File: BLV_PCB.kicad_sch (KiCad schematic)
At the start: 10 parts, among them J1 Cube0_UART_JST-PH, J2 Cube0_UART_JST-PH, J3 Cube0_UART_JST-PH, J4 Cube0_UART_Debug, J5 Cube0_UART_Debug, J6 Cube0_UART_Debug

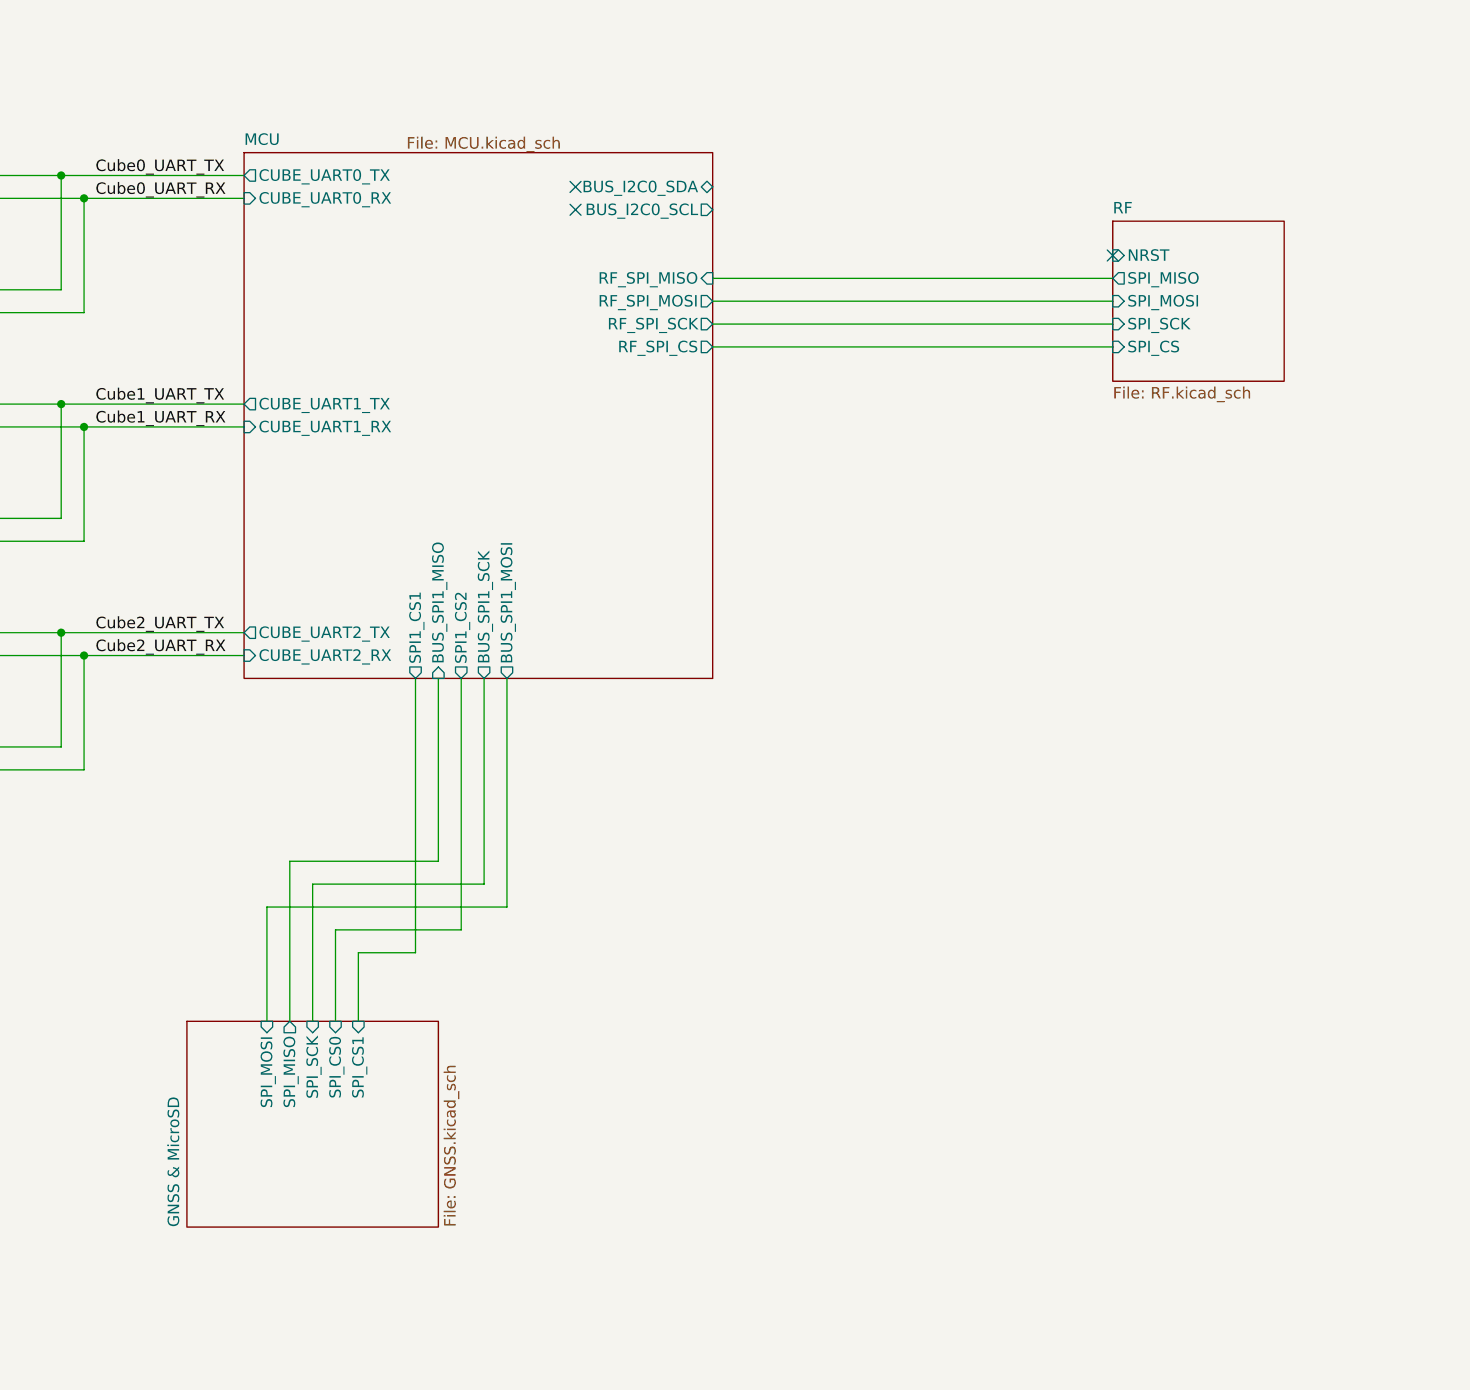
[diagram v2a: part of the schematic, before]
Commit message: Updated EBYTE placement
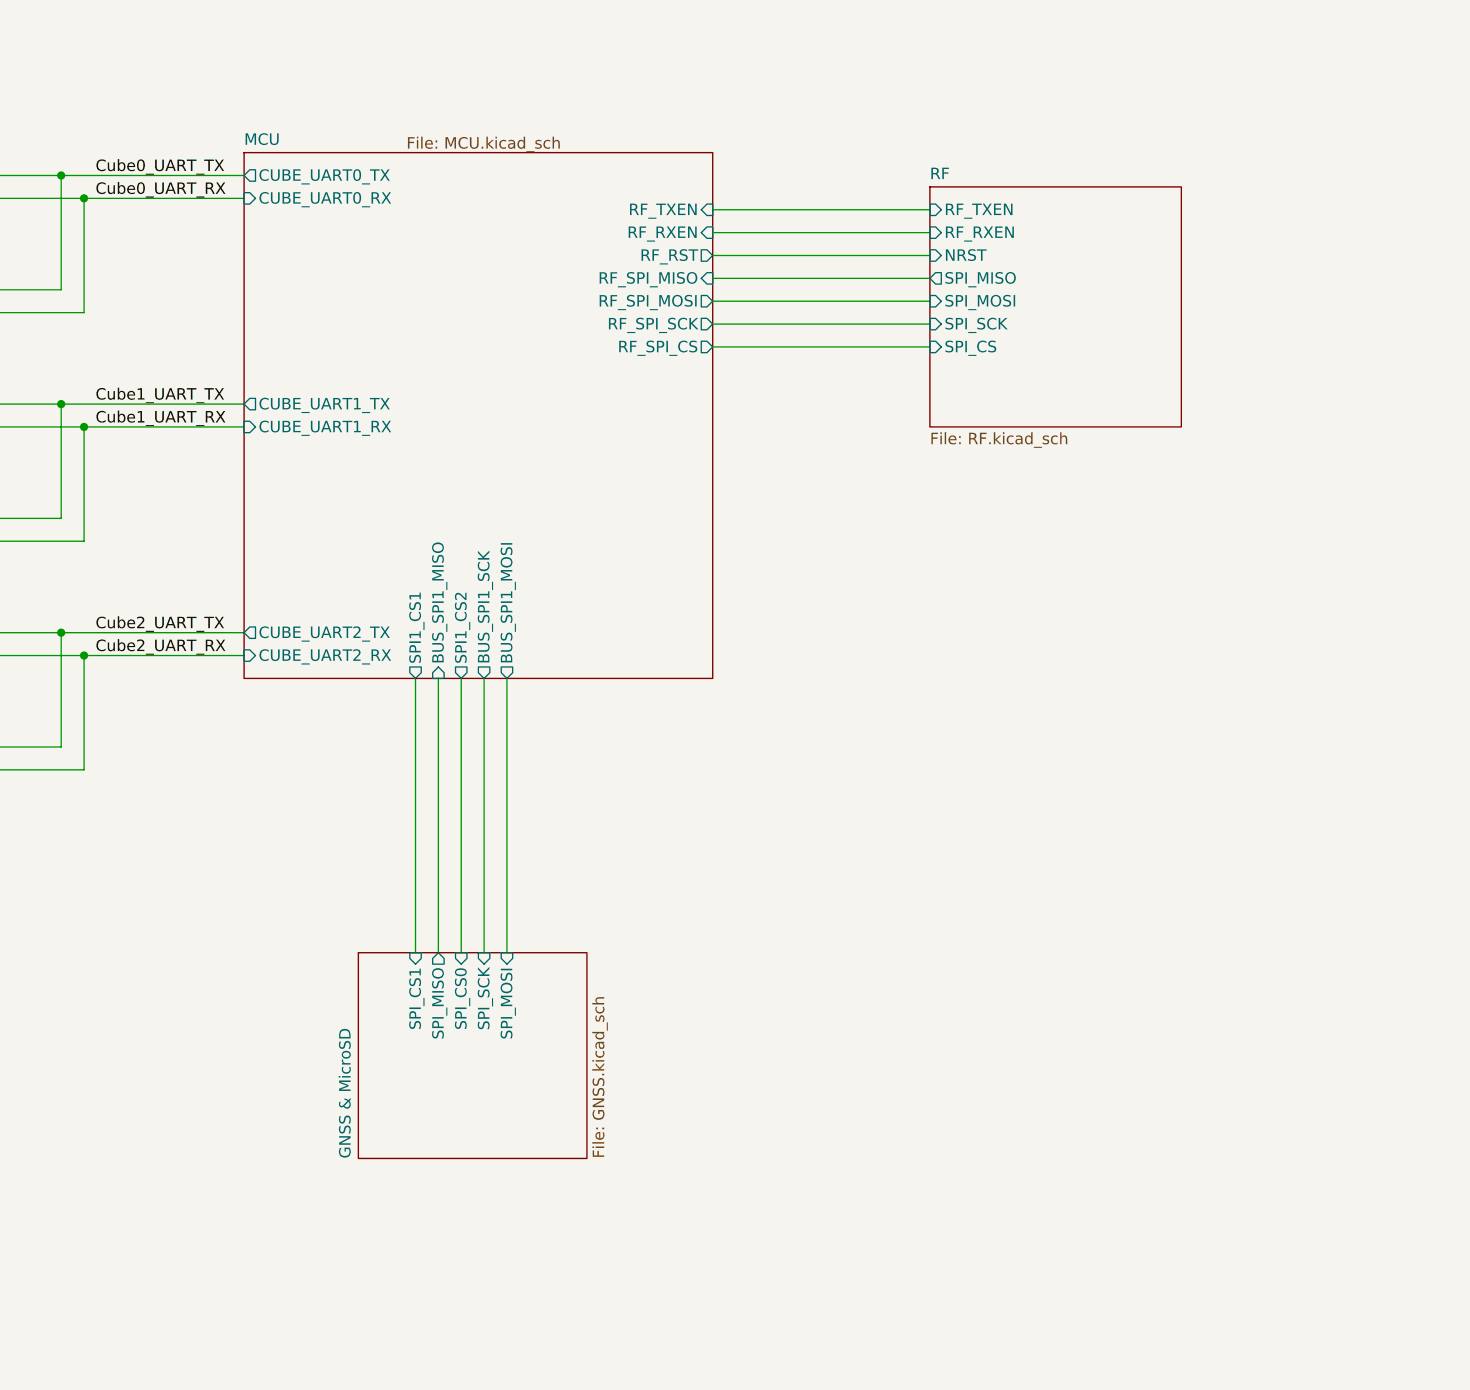
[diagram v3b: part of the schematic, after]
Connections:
- no-connect marks 6 -> 3
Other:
- sheet MCU ports: added RF_RST, RF_RXEN, RF_TXEN; removed BUS_I2C0_SCL, BUS_I2C0_SDA
- sheet RF ports: added RF_RXEN, RF_TXEN; removed none
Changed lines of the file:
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@@
-	)
-	(no_connect
-		(at 176.53 80.01)
-	)
-	(no_connect
-		(at 176.53 82.55)
-	)
-	(no_connect
-		(at 236.22 87.63)
 	)
 	(no_connect
@@
 	(wire
 		(pts
-			(xy 147.32 172.72) (xy 147.32 157.48)
-		)
-		(stroke
-			(width 0)
-			(type default)
-		)
-	)
-	(wire
-		(pts
-			(xy 142.24 172.72) (xy 142.24 160.02)
+			(xy 168.91 134.62) (xy 168.91 165.1)
 		)
 		(stroke
@@
 	(wire
 		(pts
+			(xy 191.77 92.71) (xy 215.9 92.71)
+		)
+		(stroke
+			(width 0)
+			(type default)
+		)
+	)
+	(wire
+		(pts
 			(xy 81.28 104.14) (xy 119.38 104.14)
 		)
@@
 	(wire
 		(pts
+			(xy 191.77 90.17) (xy 215.9 90.17)
+		)
+		(stroke
+			(width 0)
+			(type default)
+		)
+	)
+	(wire
+		(pts
 			(xy 93.98 121.92) (xy 95.25 121.92)
 		)
@@
 	(wire
 		(pts
-			(xy 163.83 162.56) (xy 149.86 162.56)
-		)
-		(stroke
-			(width 0)
-			(type default)
-		)
-	)
-	(wire
-		(pts
 			(xy 121.92 106.68) (xy 139.7 106.68)
 		)
@@
 	(wire
 		(pts
-			(xy 149.86 162.56) (xy 149.86 172.72)
-		)
-		(stroke
-			(width 0)
-			(type default)
-		)
-	)
-	(wire
-		(pts
-			(xy 168.91 134.62) (xy 168.91 160.02)
-		)
-		(stroke
-			(width 0)
-			(type default)
-		)
-	)
-	(wire
-		(pts
-			(xy 163.83 134.62) (xy 163.83 162.56)
+			(xy 191.77 95.25) (xy 215.9 95.25)
+		)
+		(stroke
+			(width 0)
+			(type default)
+		)
+	)
+	(wire
+		(pts
+			(xy 191.77 87.63) (xy 215.9 87.63)
+		)
+		(stroke
+			(width 0)
+			(type default)
+		)
+	)
+	(wire
+		(pts
+			(xy 163.83 134.62) (xy 163.83 165.1)
 		)
 		(stroke
@@
 	(wire
 		(pts
-			(xy 144.78 154.94) (xy 161.29 154.94)
-		)
-		(stroke
-			(width 0)
-			(type default)
-		)
-	)
-	(wire
-		(pts
-			(xy 142.24 160.02) (xy 168.91 160.02)
-		)
-		(stroke
-			(width 0)
-			(type default)
-		)
-	)
-	(wire
-		(pts
 			(xy 81.28 106.68) (xy 121.92 106.68)
 		)
@@
 	(wire
 		(pts
-			(xy 191.77 95.25) (xy 236.22 95.25)
-		)
-		(stroke
-			(width 0)
-			(type default)
-		)
-	)
-	(wire
-		(pts
 			(xy 81.28 86.36) (xy 82.55 86.36)
 		)
@@
 	(wire
 		(pts
-			(xy 166.37 134.62) (xy 166.37 157.48)
+			(xy 191.77 85.09) (xy 215.9 85.09)
+		)
+		(stroke
+			(width 0)
+			(type default)
+		)
+	)
+	(wire
+		(pts
+			(xy 166.37 134.62) (xy 166.37 165.1)
 		)
 		(stroke
@@
 	(wire
 		(pts
-			(xy 161.29 134.62) (xy 161.29 154.94)
+			(xy 161.29 134.62) (xy 161.29 165.1)
 		)
 		(stroke
@@
 	(wire
 		(pts
-			(xy 191.77 97.79) (xy 236.22 97.79)
+			(xy 191.77 82.55) (xy 215.9 82.55)
 		)
 		(stroke
@@
 	(wire
 		(pts
-			(xy 152.4 172.72) (xy 152.4 165.1)
-		)
-		(stroke
-			(width 0)
-			(type default)
-		)
-	)
-	(wire
-		(pts
 			(xy 121.92 81.28) (xy 121.92 93.98)
 		)
@@
 	(wire
 		(pts
-			(xy 152.4 165.1) (xy 158.75 165.1)
-		)
-		(stroke
-			(width 0)
-			(type default)
-		)
-	)
-	(wire
-		(pts
-			(xy 147.32 157.48) (xy 166.37 157.48)
-		)
-		(stroke
-			(width 0)
-			(type default)
-		)
-	)
-	(wire
-		(pts
-			(xy 191.77 90.17) (xy 236.22 90.17)
+			(xy 191.77 97.79) (xy 215.9 97.79)
 		)
 		(stroke
@@
 		(pts
 			(xy 119.38 104.14) (xy 139.7 104.14)
-		)
-		(stroke
-			(width 0)
-			(type default)
-		)
-	)
-	(wire
-		(pts
-			(xy 191.77 92.71) (xy 236.22 92.71)
-		)
-		(stroke
-			(width 0)
-			(type default)
-		)
-	)
-	(wire
-		(pts
-			(xy 144.78 172.72) (xy 144.78 154.94)
 		)
 		(stroke
@@
 			)
 		)
-		(pin "BUS_I2C0_SCL" output
-			(at 191.77 82.55 0)
-			(effects
-				(font
-					(size 1.27 1.27)
-				)
-				(justify right)
-			)
-		)
-		(pin "BUS_I2C0_SDA" bidirectional
-			(at 191.77 80.01 0)
-			(effects
-				(font
-					(size 1.27 1.27)
-				)
-				(justify right)
-			)
-		)
 		(pin "RF_SPI_CS" output
 			(at 191.77 97.79 0)
@@
 				)
 				(justify left)
+			)
+		)
+		(pin "RF_RST" output
+			(at 191.77 87.63 0)
+			(effects
+				(font
+					(size 1.27 1.27)
+				)
+				(justify right)
+			)
+		)
+		(pin "RF_RXEN" input
+			(at 191.77 85.09 0)
+			(effects
+				(font
+					(size 1.27 1.27)
+				)
+				(justify right)
+			)
+		)
+		(pin "RF_TXEN" input
+			(at 191.77 82.55 0)
+			(effects
+				(font
+					(size 1.27 1.27)
+				)
+				(justify right)
 			)
 		)
@@
 	)
 	(sheet
-		(at 236.22 83.82)
-		(size 19.05 17.78)
+		(at 215.9 80.01)
+		(size 27.94 26.67)
 		(exclude_from_sim no)
 		(in_bom yes)
@@
 		)
 		(property "Sheetname" "RF"
-			(at 236.22 83.1084 0)
+			(at 215.9 79.2984 0)
 			(effects
 				(font
@@
 		)
 		(property "Sheetfile" "RF.kicad_sch"
-			(at 236.22 102.1846 0)
+			(at 215.9 107.2646 0)
 			(effects
 				(font
@@
 		)
 		(property "Field2" ""
-			(at 236.22 83.82 0)
+			(at 215.9 80.01 0)
 			(effects
 				(font
@@
 		)
 		(pin "NRST" input
-			(at 236.22 87.63 180)
+			(at 215.9 87.63 180)
 			(effects
 				(font
@@
 		)
 		(pin "SPI_CS" input
-			(at 236.22 97.79 180)
+			(at 215.9 97.79 180)
 			(effects
 				(font
@@
 		)
 		(pin "SPI_MISO" output
-			(at 236.22 90.17 180)
+			(at 215.9 90.17 180)
 			(effects
 				(font
@@
 		)
 		(pin "SPI_MOSI" input
-			(at 236.22 92.71 180)
+			(at 215.9 92.71 180)
 			(effects
 				(font
@@
 		)
 		(pin "SPI_SCK" input
-			(at 236.22 95.25 180)
+			(at 215.9 95.25 180)
+			(effects
+				(font
+					(size 1.27 1.27)
+				)
+				(justify left)
+			)
+		)
+		(pin "RF_RXEN" input
+			(at 215.9 85.09 180)
+			(effects
+				(font
+					(size 1.27 1.27)
+				)
+				(justify left)
+			)
+		)
+		(pin "RF_TXEN" input
+			(at 215.9 82.55 180)
 			(effects
 				(font
@@
 	)
 	(sheet
-		(at 133.35 172.72)
-		(size 27.94 22.86)
+		(at 152.4 165.1)
+		(size 25.4 22.86)
 		(exclude_from_sim no)
 		(in_bom yes)
@@
 		)
 		(property "Sheetname" "GNSS & MicroSD"
-			(at 132.6384 195.58 90)
+			(at 151.6884 187.96 90)
 			(effects
 				(font
@@
 		)
 		(property "Sheetfile" "GNSS.kicad_sch"
-			(at 161.8746 195.58 90)
+			(at 178.3846 187.96 90)
 			(effects
 				(font
@@
 		)
 		(pin "SPI_MISO" output
-			(at 144.78 172.72 90)
+			(at 161.29 165.1 90)
 			(effects
 				(font
@@
 		)
 		(pin "SPI_MOSI" input
-			(at 142.24 172.72 90)
+			(at 168.91 165.1 90)
 			(effects
 				(font
@@
 		)
 		(pin "SPI_SCK" input
-			(at 147.32 172.72 90)
+			(at 166.37 165.1 90)
 			(effects
 				(font
@@
 		)
 		(pin "SPI_CS0" input
-			(at 149.86 172.72 90)
+			(at 163.83 165.1 90)
 			(effects
 				(font
@@
 		)
 		(pin "SPI_CS1" input
-			(at 152.4 172.72 90)
-			(effects
-				(font
+			(at 158.75 165.1 90)
+			(effects
+				(font
